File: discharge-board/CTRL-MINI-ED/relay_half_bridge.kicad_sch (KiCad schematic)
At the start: 10 parts, among them K1 G2RL-1A-E, K2 G2RL-1A-E, Q1 Q_NMOS_GSD, Q2 Q_NMOS_GSD

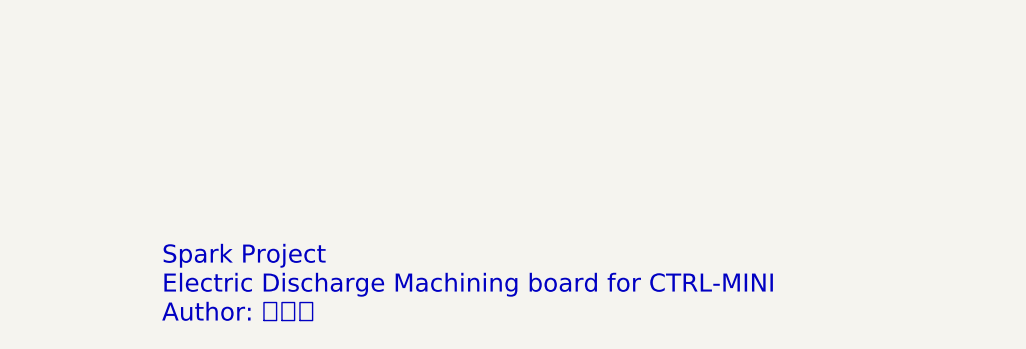
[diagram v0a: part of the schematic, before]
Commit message: Add PWM voltage divider and refactor
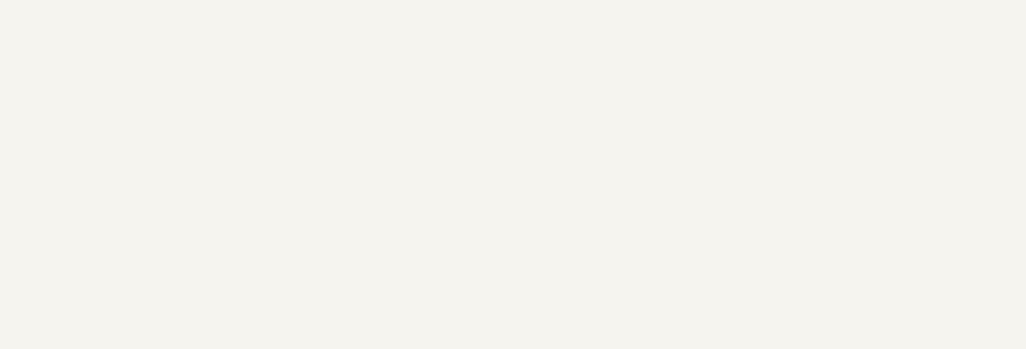
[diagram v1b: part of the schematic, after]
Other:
- note removed: "Spark Project Electric Discharge Machining board for CTRL-MINI Author: 夕月霞"
- company: (none) -> Spark Project
- title: (none) -> CTRL-MINI-ED
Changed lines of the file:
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@@
 	(generator_version "8.0")
 	(paper "A4")
+	(title_block
+		(title "CTRL-MINI-ED")
+		(date "2024-12-11")
+		(rev "2")
+		(company "Spark Project")
+		(comment 1 "Author: 夕月霞 (xyx)")
+		(comment 2 "Electric Discharge Machining board for CTRL-MINI")
+	)
 	(junction
 		(at 106.68 114.3)
@@
 	)
 	(image
-		(at 184.15 173.99)
+		(at 276.86 173.99)
+		(scale 1.13867)
 		(data "iVBORw0KGgoAAAANSUhEUgAAATsAAAEsCAYAAAC8DxTkAAAACXBIWXMAAHc0AAB3NAG21TCYAAAA"
 			"GXRFWHRTb2Z0d2FyZQB3d3cuaW5rc2NhcGUub3Jnm+48GgAAIABJREFUeJzt3XmcXFWZ//HPc6u6"
@@
 		)
 	)
-	(text "Spark Project\nElectric Discharge Machining board for CTRL-MINI\nAuthor: 夕月霞"
-		(exclude_from_sim yes)
-		(at 192.024 169.672 0)
-		(effects
-			(font
-				(size 2 2)
-				(color 132 0 0 1)
-			)
-			(justify left top)
-		)
-	)
